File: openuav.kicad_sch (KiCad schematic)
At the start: 69 parts, among them J1 Conn_01x01, J10 Conn_01x01, J11 Conn_01x01, J12 Conn_01x01, J13 Conn_01x01, J14 Conn_01x01, J15 Conn_01x01, J16 Conn_01x01, J17 Conn_01x01, J18 Conn_01x01, J19 Conn_01x01, J2 Conn_01x01, J20 Conn_01x01, J21 Conn_01x01, J22 Conn_01x01, J23 Conn_01x01, J24 Conn_01x01, J25 Conn_01x01, J26 Conn_01x01, J27 Conn_01x01, J28 Conn_01x01, J29 Conn_01x01, J3 Conn_01x01, J30 Conn_01x01, J31 Conn_01x01, J32 Conn_01x01, J33 Conn_01x01, J34 Conn_01x01, J35 Conn_01x01, J4 Conn_01x01, J5 Conn_01x01, J6 Conn_01x01, J7 Conn_01x01, J8 Conn_01x01, J9 Conn_01x01, J99 USB_C_Receptacle_USB2.0, U1 STM32G431CBUx, U3 LSM6DSR, U4 LPS22HH, U5 TPS54202DDC, U6 W25N01GVZEIG, U7 XC6206P332MR

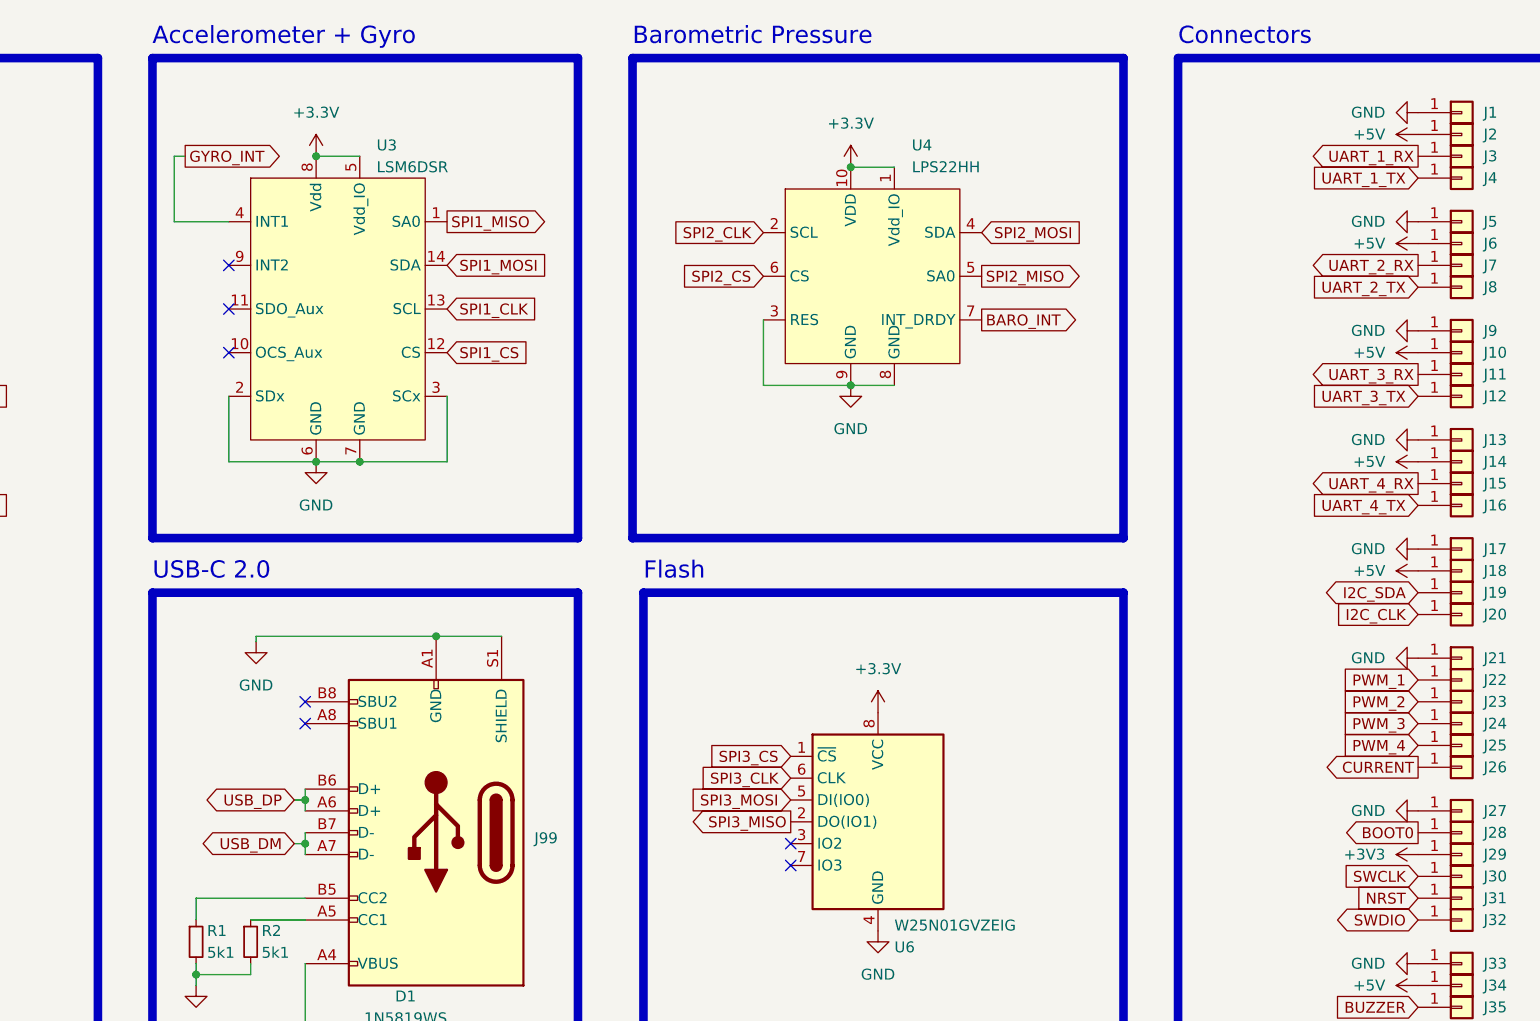
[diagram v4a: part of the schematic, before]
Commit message: fix 3v3/3.3v confusion, make gyro pinout compatble with BMI270
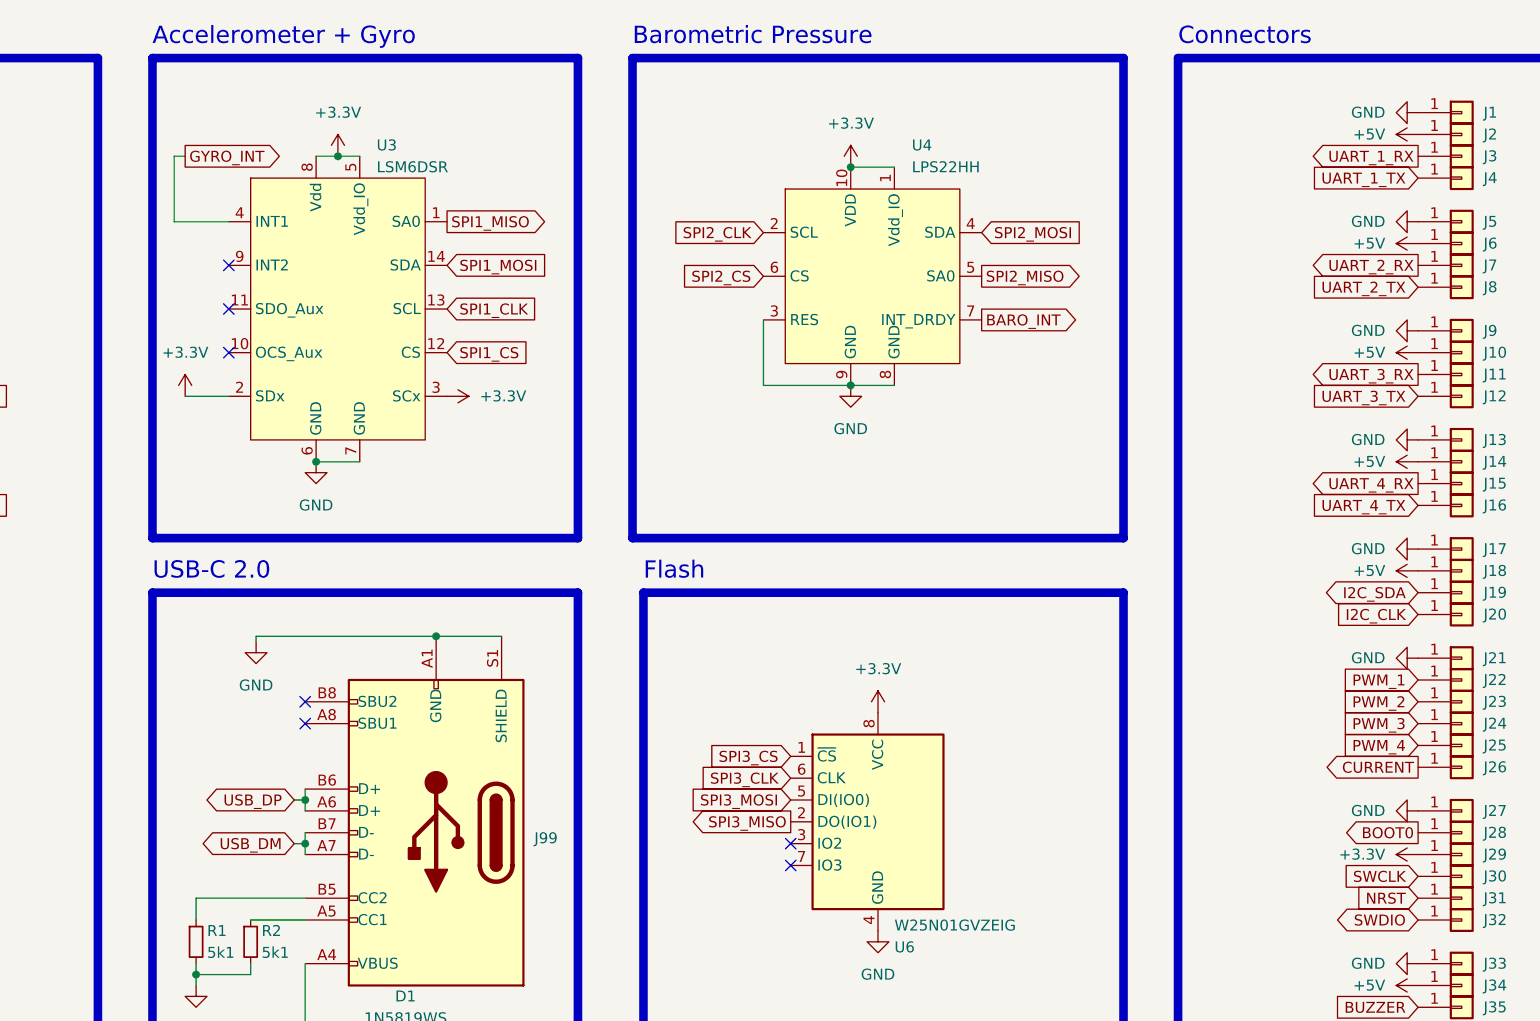
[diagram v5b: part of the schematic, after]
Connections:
- net +3V3: now also U3.2 (SDx), U3.3 (SCx)
- net GND: no longer U3.2 (SDx), U3.3 (SCx)
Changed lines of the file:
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@@
   (junction (at 54.61 33.02) (diameter 0) (color 0 0 0 0)
   )
-  (junction (at 123.19 35.56) (diameter 0) (color 0 0 0 0)
-  )
   (junction (at 121.92 115.57) (diameter 0) (color 0 0 0 0)
   )
@@
   (junction (at 194.31 173.99) (diameter 0) (color 0 0 0 0)
   )
-  (junction (at 128.27 71.12) (diameter 0) (color 0 0 0 0)
-  )
   (junction (at 34.29 43.18) (diameter 0) (color 0 0 0 0)
   )
@@
   (junction (at 56.515 167.64) (diameter 0) (color 0 0 0 0)
   )
+  (junction (at 125.73 35.56) (diameter 0) (color 0 0 0 0)
+  )
   (junction (at 259.334 170.18) (diameter 0) (color 0 0 0 0)
   )
@@
     (stroke (width 0) (type default))
   )
+  (wire (pts (xy 125.73 35.56) (xy 128.27 35.56))
+    (stroke (width 0) (type default))
+  )
   (wire (pts (xy 256.794 170.18) (xy 259.334 170.18))
     (stroke (width 0) (type default))
@@
     (stroke (width 0) (type default))
   )
-  (wire (pts (xy 123.19 35.56) (xy 128.27 35.56))
-    (stroke (width 0) (type default))
-  )
-  (wire (pts (xy 113.03 63.5) (xy 113.03 71.12))
+  (wire (pts (xy 123.19 35.56) (xy 125.73 35.56))
     (stroke (width 0) (type default))
   )
@@
     (stroke (width 0) (type default))
   )
+  (wire (pts (xy 107.95 63.5) (xy 113.03 63.5))
+    (stroke (width 0) (type default))
+  )
   (wire (pts (xy 91.44 175.26) (xy 91.44 177.8))
     (stroke (width 0) (type default))
@@
     (stroke (width 0) (type default))
   )
-  (wire (pts (xy 128.27 71.12) (xy 138.43 71.12))
-    (stroke (width 0) (type default))
-  )
   (wire (pts (xy 163.83 168.91) (xy 173.99 168.91))
     (stroke (width 0) (type default))
@@
     (stroke (width 0) (type default))
   )
-  (wire (pts (xy 113.03 71.12) (xy 123.19 71.12))
-    (stroke (width 0) (type default))
-  )
   (wire (pts (xy 175.26 62.23) (xy 175.26 54.61))
     (stroke (width 0) (type default))
@@
     (stroke (width 0) (type default))
   )
-  (wire (pts (xy 138.43 71.12) (xy 138.43 63.5))
-    (stroke (width 0) (type default))
-  )
   (wire (pts (xy 121.92 129.54) (xy 121.92 138.43))
     (stroke (width 0) (type default))
@@
     )
   )
+  (symbol (lib_id "power:+3.3V") (at 138.43 63.5 270) (unit 1)
+    (in_bom yes) (on_board yes) (dnp no)
+    (property "Reference" "#PWR024" (at 134.62 63.5 0)
+      (effects (font (size 1.27 1.27)) hide)
+    )
+    (property "Value" "+3.3V" (at 142.24 63.5 90)
+      (effects (font (size 1.27 1.27)) (justify left))
+    )
+    (property "Footprint" "" (at 138.43 63.5 0)
+      (effects (font (size 1.27 1.27)) hide)
+    )
+    (property "Datasheet" "" (at 138.43 63.5 0)
+      (effects (font (size 1.27 1.27)) hide)
+    )
+    (pin "1")
+    (instances
+      (project "openuav"
+        (path "/e63e39d7-6ac0-4ffd-8aa3-1841a4541b55"
+          (reference "#PWR024") (unit 1)
+        )
+      )
+    )
+  )
   (symbol (lib_name "GND_1") (lib_id "power:GND") (at 251.46 81.28 270) (unit 1)
     (in_bom yes) (on_board yes) (dnp no)
@@
     )
   )
-  (symbol (lib_id "power:+3.3V") (at 123.19 35.56 0) (unit 1)
-    (in_bom yes) (on_board yes) (dnp no) (fields_autoplaced)
-    (property "Reference" "#PWR011" (at 123.19 39.37 0)
-      (effects (font (size 1.27 1.27)) hide)
-    )
-    (property "Value" "+3.3V" (at 123.19 30.48 0)
-      (effects (font (size 1.27 1.27)))
-    )
-    (property "Footprint" "" (at 123.19 35.56 0)
-      (effects (font (size 1.27 1.27)) hide)
-    )
-    (property "Datasheet" "" (at 123.19 35.56 0)
-      (effects (font (size 1.27 1.27)) hide)
-    )
-    (pin "1")
-    (instances
-      (project "openuav"
-        (path "/e63e39d7-6ac0-4ffd-8aa3-1841a4541b55"
-          (reference "#PWR011") (unit 1)
-        )
-      )
-    )
-  )
   (symbol (lib_id "Device:C_Small") (at 34.29 40.64 0) (unit 1)
     (in_bom yes) (on_board yes) (dnp no) (fields_autoplaced)
@@
     )
   )
+  (symbol (lib_id "power:+3.3V") (at 125.73 35.56 0) (unit 1)
+    (in_bom yes) (on_board yes) (dnp no) (fields_autoplaced)
+    (property "Reference" "#PWR011" (at 125.73 39.37 0)
+      (effects (font (size 1.27 1.27)) hide)
+    )
+    (property "Value" "+3.3V" (at 125.73 30.48 0)
+      (effects (font (size 1.27 1.27)))
+    )
+    (property "Footprint" "" (at 125.73 35.56 0)
+      (effects (font (size 1.27 1.27)) hide)
+    )
+    (property "Datasheet" "" (at 125.73 35.56 0)
+      (effects (font (size 1.27 1.27)) hide)
+    )
+    (pin "1")
+    (instances
+      (project "openuav"
+        (path "/e63e39d7-6ac0-4ffd-8aa3-1841a4541b55"
+          (reference "#PWR011") (unit 1)
+        )
+      )
+    )
+  )
   (symbol (lib_id "Connector:USB_C_Receptacle_USB2.0") (at 137.16 114.3 180) (unit 1)
     (in_bom yes) (on_board yes) (dnp no) (fields_autoplaced)
@@
     )
   )
+  (symbol (lib_id "power:+3.3V") (at 251.46 116.84 90) (unit 1)
+    (in_bom yes) (on_board yes) (dnp no)
+    (property "Reference" "#PWR031" (at 255.27 116.84 0)
+      (effects (font (size 1.27 1.27)) hide)
+    )
+    (property "Value" "+3.3V" (at 247.65 116.84 90)
+      (effects (font (size 1.27 1.27)) (justify left))
+    )
+    (property "Footprint" "" (at 251.46 116.84 0)
+      (effects (font (size 1.27 1.27)) hide)
+    )
+    (property "Datasheet" "" (at 251.46 116.84 0)
+      (effects (font (size 1.27 1.27)) hide)
+    )
+    (pin "1")
+    (instances
+      (project "openuav"
+        (path "/e63e39d7-6ac0-4ffd-8aa3-1841a4541b55"
+          (reference "#PWR031") (unit 1)
+        )
+      )
+    )
+  )
   (symbol (lib_id "power:GND") (at 185.42 62.23 0) (unit 1)
     (in_bom yes) (on_board yes) (dnp no) (fields_autoplaced)
@@
     )
   )
+  (symbol (lib_id "power:+3.3V") (at 107.95 63.5 0) (unit 1)
+    (in_bom yes) (on_board yes) (dnp no) (fields_autoplaced)
+    (property "Reference" "#PWR026" (at 107.95 67.31 0)
+      (effects (font (size 1.27 1.27)) hide)
+    )
+    (property "Value" "+3.3V" (at 107.95 58.42 0)
+      (effects (font (size 1.27 1.27)))
+    )
+    (property "Footprint" "" (at 107.95 63.5 0)
+      (effects (font (size 1.27 1.27)) hide)
+    )
+    (property "Datasheet" "" (at 107.95 63.5 0)
+      (effects (font (size 1.27 1.27)) hide)
+    )
+    (pin "1")
+    (instances
+      (project "openuav"
+        (path "/e63e39d7-6ac0-4ffd-8aa3-1841a4541b55"
+          (reference "#PWR026") (unit 1)
+        )
+      )
+    )
+  )
   (symbol (lib_id "Connector_Generic:Conn_01x01") (at 256.54 101.6 0) (unit 1)
     (in_bom yes) (on_board yes) (dnp no)
@@
         )
       )
-    )
-  )
-  (symbol (lib_id "power:+3V3") (at 251.46 116.84 90) (unit 1)
-    (in_bom yes) (on_board yes) (dnp no)
-    (property "Reference" "#PWR026" (at 255.27 116.84 0)
-      (effects (font (size 1.27 1.27)) hide)
-    )
-    (property "Value" "+3V3" (at 247.65 116.84 90)
-      (effects (font (size 1.27 1.27)) (justify left))
-    )
-    (property "Footprint" "" (at 251.46 116.84 0)
-      (effects (font (size 1.27 1.27)) hide)
-    )
-    (property "Datasheet" "" (at 251.46 116.84 0)
-      (effects (font (size 1.27 1.27)) hide)
-    )
-    (pin "1")
-    (instances
-      (project "openuav"
-        (path "/e63e39d7-6ac0-4ffd-8aa3-1841a4541b55"
-          (reference "#PWR026") (unit 1)
-        )
-      )

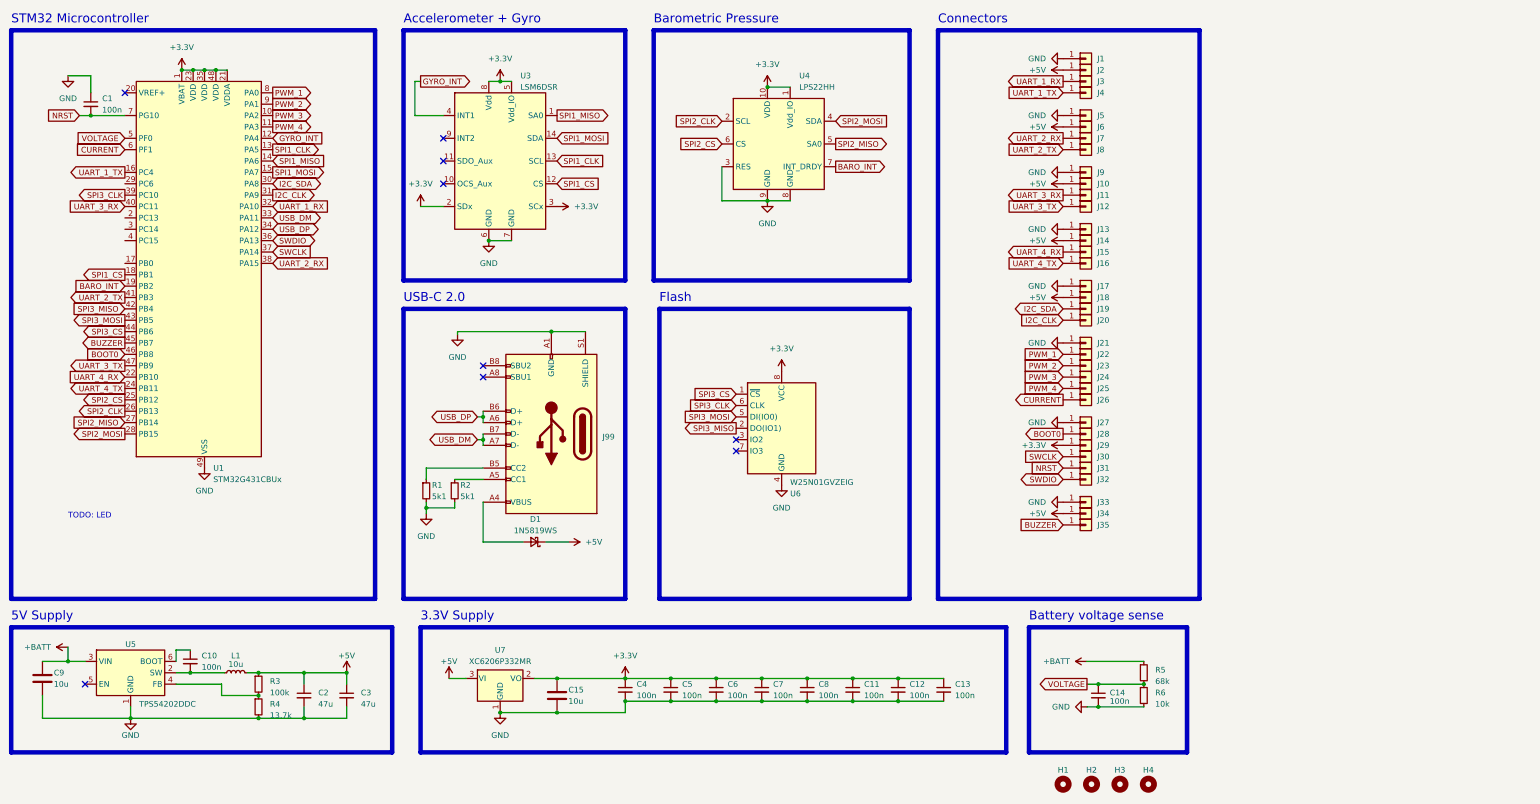
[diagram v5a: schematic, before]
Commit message: Improve connector spacing and thermal management
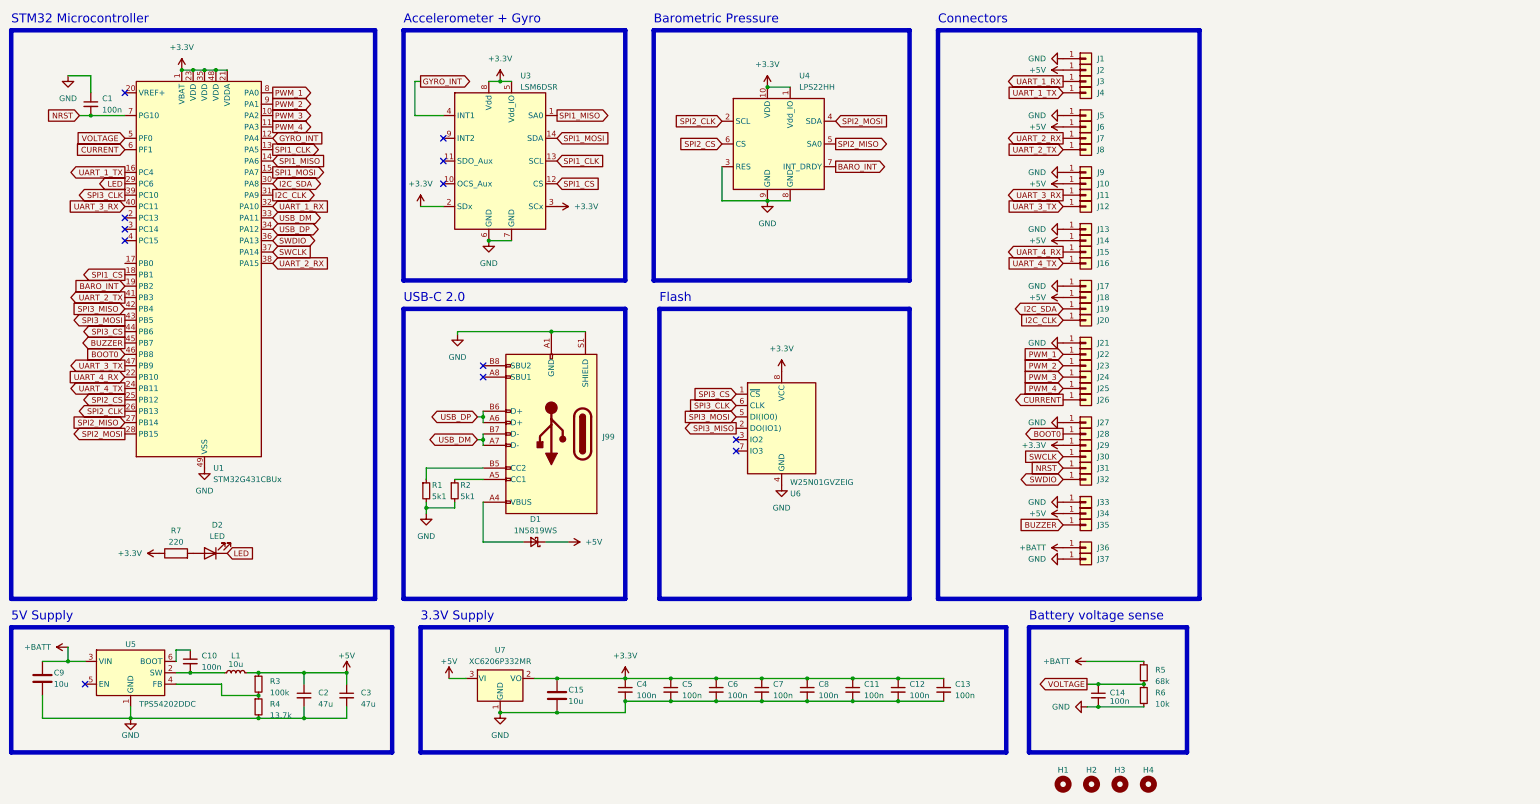
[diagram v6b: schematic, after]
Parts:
- added D2: LED, LED_SMD:LED_0603_1608Metric, symbol Device:LED
- added J36, J37: Conn_01x01, Connector_Custom_Pads:TP-2.54, symbol Connector_Generic:Conn_01x01
- added R7: 220, Resistor_SMD:R_0805_2012Metric, symbol Device:R
- J1, J10, J11, J12, J13, J14, J15, J16, J17, J18, J19, J2, J20, J21, J22, J23, J24, J25, J26, J27, J28, J29, J3, J30, J31, J32, J33, J34, J35, J4, J5, J6, J7, J8, J9: footprint TestPoint:TestPoint_THTPad_1.5x1.5mm_Drill0.7mm -> Connector_Custom_Pads:TP-2.54
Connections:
- net +3V3: now also R7.1
- net +BATT: now also J36.1 (Pin_1)
- net GND: now also J37.1 (Pin_1)
- net LED: now reaches U1.29 (PC6)
- net LED: now also D2.1 (K)
- new net: D2.2 (A), R7.2
- no-connect marks 9 -> 12
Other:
- note removed: "TODO: LED"
